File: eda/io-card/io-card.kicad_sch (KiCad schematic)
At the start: 22 parts, among them J3 PortA, J4 PortB, J5 ControlLines, J6 SPI, U1 W65C22SxP, U12 74HCT00, U2 W65C22SxP, U3 74HCT14, U4 74HCT14, U5 74HCT14, U8 74HCT138

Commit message: Add expansion backplane
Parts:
- removed H3, H4: MountingHole, MountingHole:MountingHole_2.5mm, symbol Mechanical:MountingHole
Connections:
- net at U2.7 (PA5): now also U8.3 (A2); no longer U8.1 (A0)
- net at U2.9 (PA7): now also U8.1 (A0); no longer U8.3 (A2)

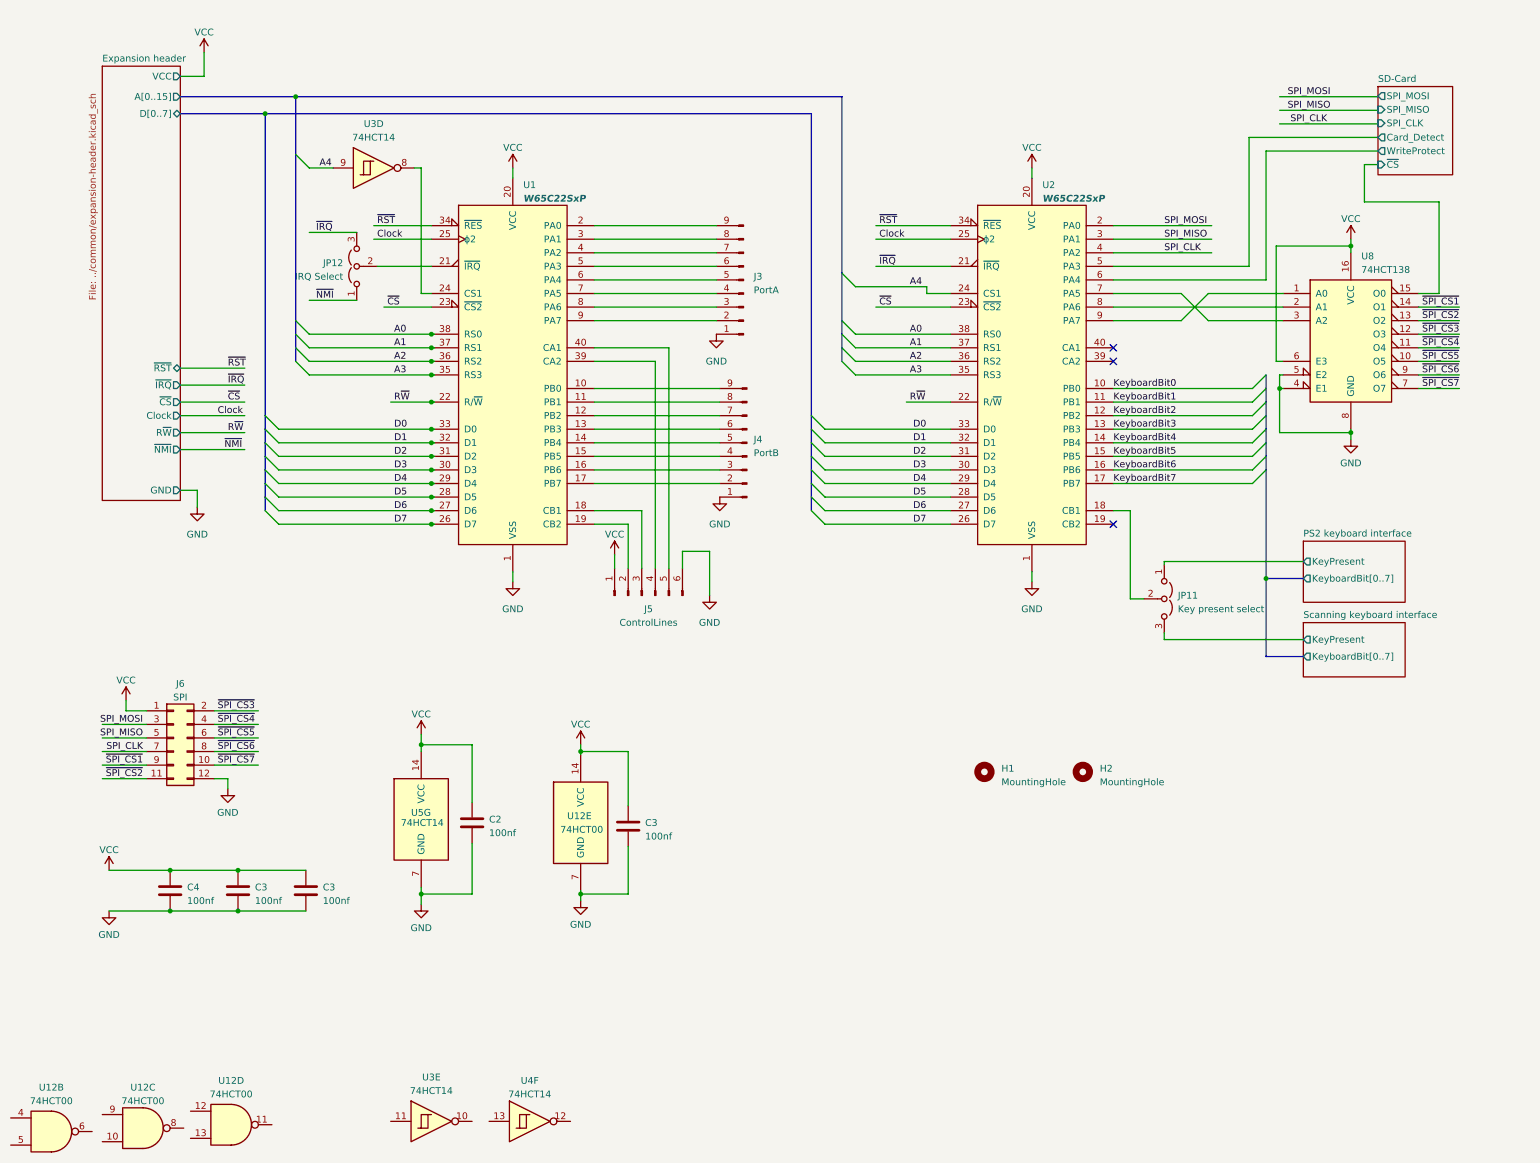
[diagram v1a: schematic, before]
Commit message: EDA work for new expansion header
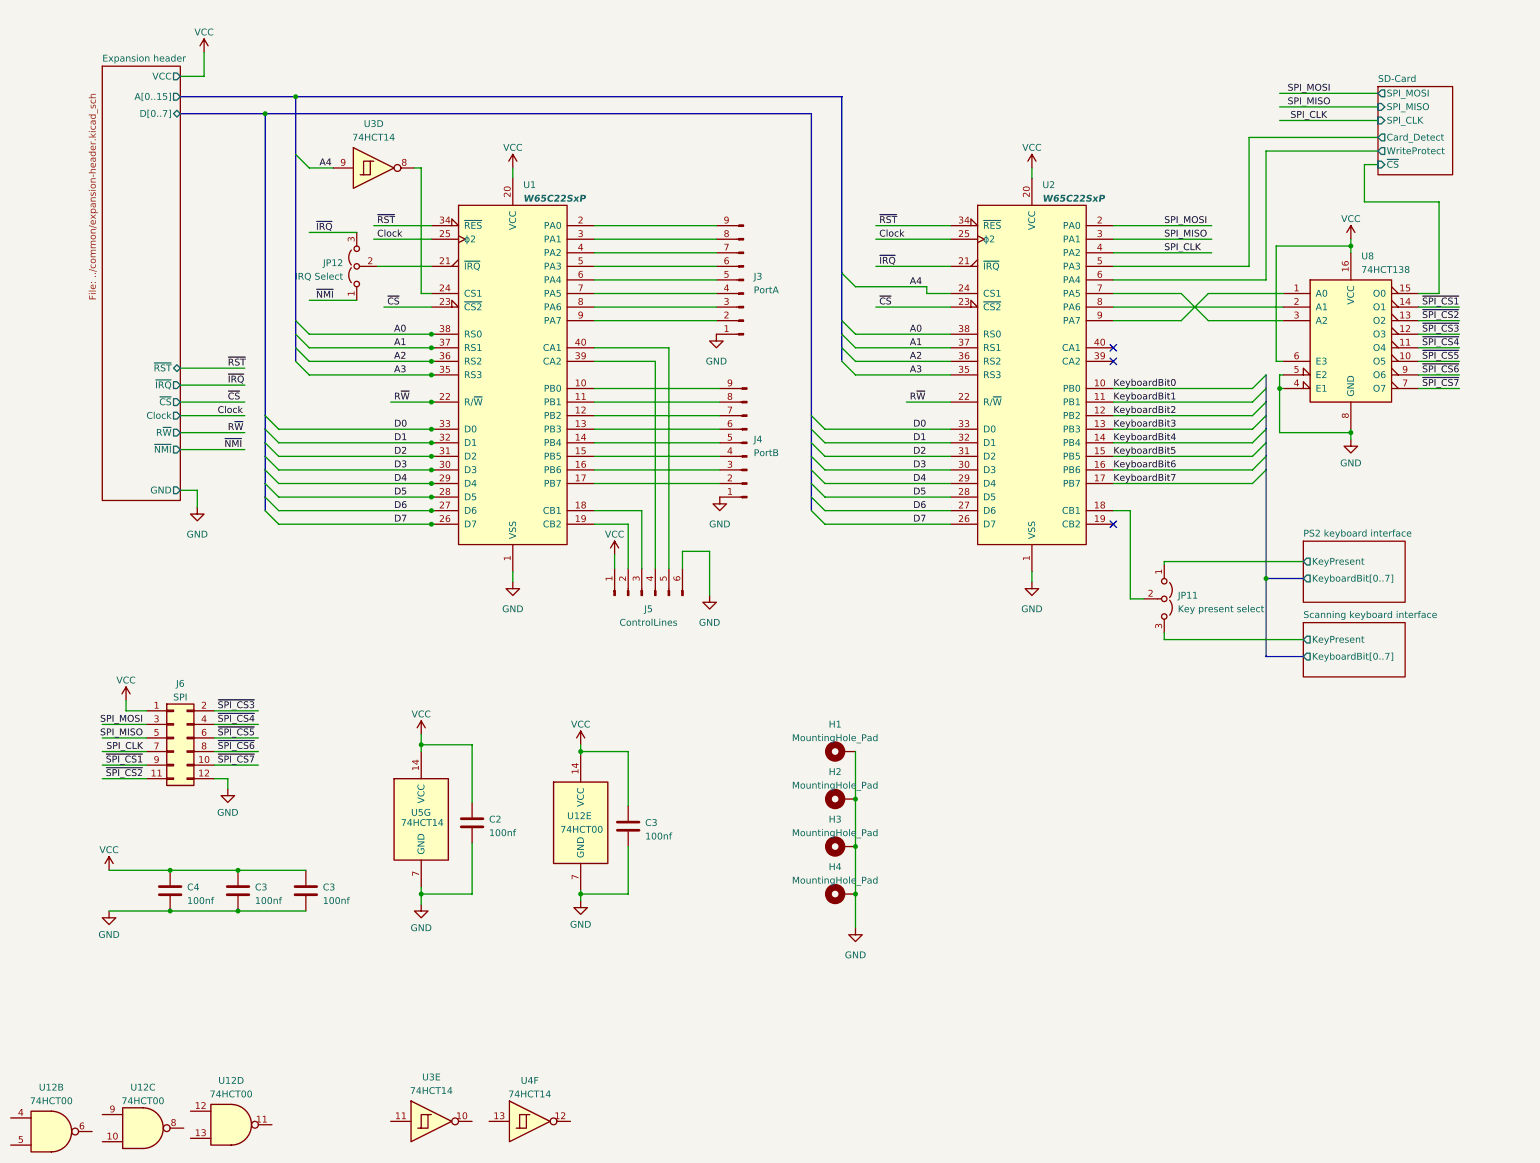
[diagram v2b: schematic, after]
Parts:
- removed H1, H2: MountingHole, MountingHole:MountingHole_2.5mm, symbol Mechanical:MountingHole
- added H1, H2, H3, H4: MountingHole_Pad, MountingHole:MountingHole_2.5mm_Pad, symbol Mechanical:MountingHole_Pad
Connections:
- net GND: now also H1.1, H2.1, H3.1, H4.1

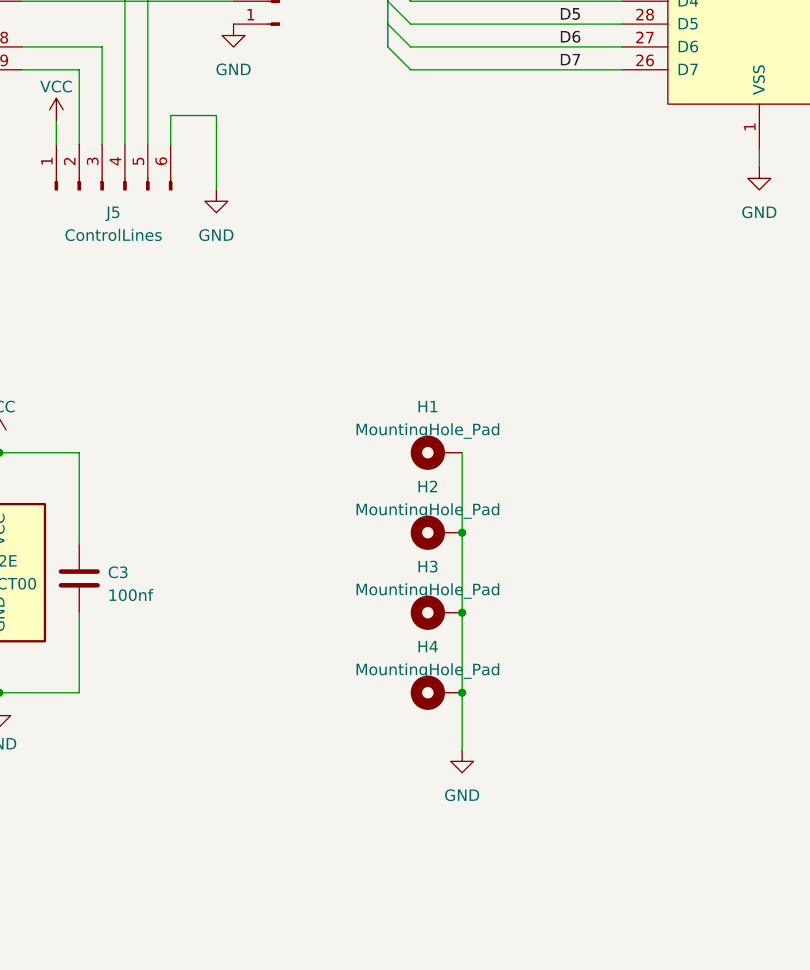
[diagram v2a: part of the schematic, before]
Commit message: Generate step files and start on gpu for new board layout
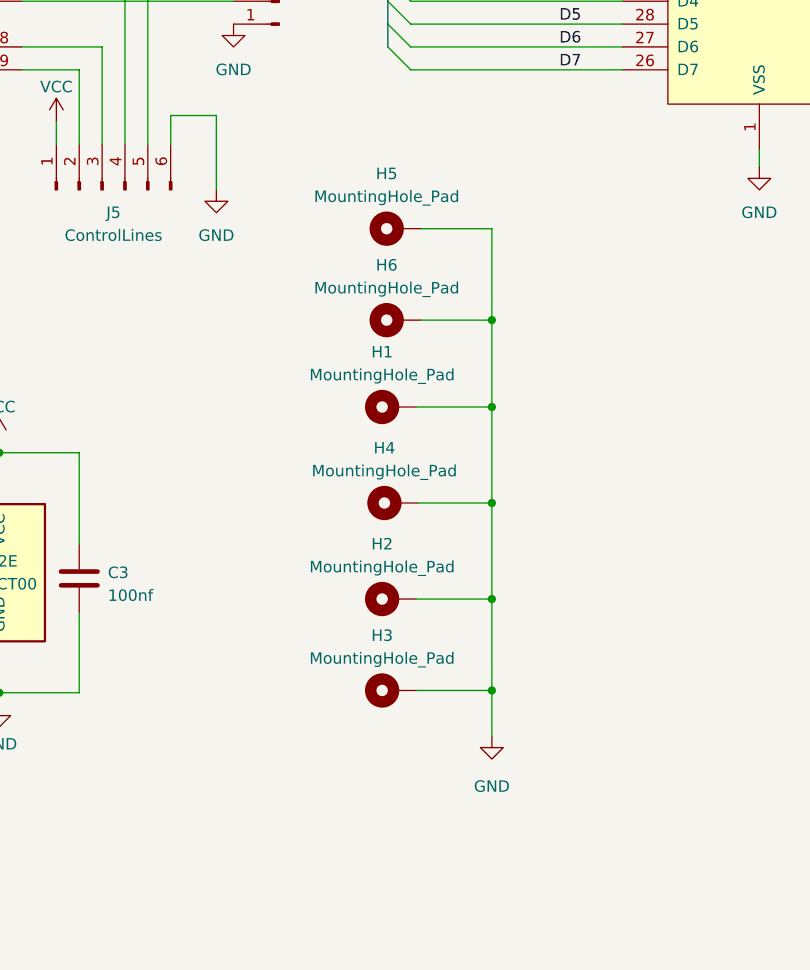
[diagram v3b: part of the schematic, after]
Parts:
- added H5, H6: MountingHole_Pad, MountingHole:MountingHole_2.5mm_Pad_Via, symbol Mechanical:MountingHole_Pad
- H1, H2, H3, H4: footprint MountingHole:MountingHole_2.5mm_Pad -> MountingHole:MountingHole_2.5mm_Pad_Via
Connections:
- net GND: now also H5.1, H6.1

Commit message: Normalize cap size
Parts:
- C2, C3, C4: footprint Capacitor_THT:C_Disc_D3.4mm_W2.1mm_P2.50mm -> Capacitor_THT:C_Disc_D3.8mm_W2.6mm_P2.50mm
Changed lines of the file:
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@@
       (effects (font (size 1.27 1.27)) (justify left))
     )
-    (property "Footprint" "Capacitor_THT:C_Disc_D3.4mm_W2.1mm_P2.50mm" (at 99.3902 173.355 0)
+    (property "Footprint" "Capacitor_THT:C_Disc_D3.8mm_W2.6mm_P2.50mm" (at 99.3902 173.355 0)
       (effects (font (size 1.27 1.27)) hide)
     )
@@
       (effects (font (size 1.27 1.27)) (justify left))
     )
-    (property "Footprint" "Capacitor_THT:C_Disc_D3.4mm_W2.1mm_P2.50mm" (at 55.5752 186.055 0)
+    (property "Footprint" "Capacitor_THT:C_Disc_D3.8mm_W2.6mm_P2.50mm" (at 55.5752 186.055 0)
       (effects (font (size 1.27 1.27)) hide)
     )
@@
       (effects (font (size 1.27 1.27)) (justify left))
     )
-    (property "Footprint" "Capacitor_THT:C_Disc_D3.4mm_W2.1mm_P2.50mm" (at 128.6002 173.99 0)
+    (property "Footprint" "Capacitor_THT:C_Disc_D3.8mm_W2.6mm_P2.50mm" (at 128.6002 173.99 0)
       (effects (font (size 1.27 1.27)) hide)
     )
@@
       (effects (font (size 1.27 1.27)) (justify left))
     )
-    (property "Footprint" "Capacitor_THT:C_Disc_D3.4mm_W2.1mm_P2.50mm" (at 42.8752 186.055 0)
+    (property "Footprint" "Capacitor_THT:C_Disc_D3.8mm_W2.6mm_P2.50mm" (at 42.8752 186.055 0)
       (effects (font (size 1.27 1.27)) hide)
     )
@@
       (effects (font (size 1.27 1.27)) (justify left))
     )
-    (property "Footprint" "Capacitor_THT:C_Disc_D3.4mm_W2.1mm_P2.50mm" (at 68.2752 186.055 0)
-      (effects (font (size 1.27 1.27)) hide)
-    )
+    (property "Footprint" "Capacitor_THT:C_Disc_D3.8mm_W2.6mm_P2.50mm" (at 68.2752 186.055 0)
+      (effects (font (size 1.27 1.27)) hide)
+    )

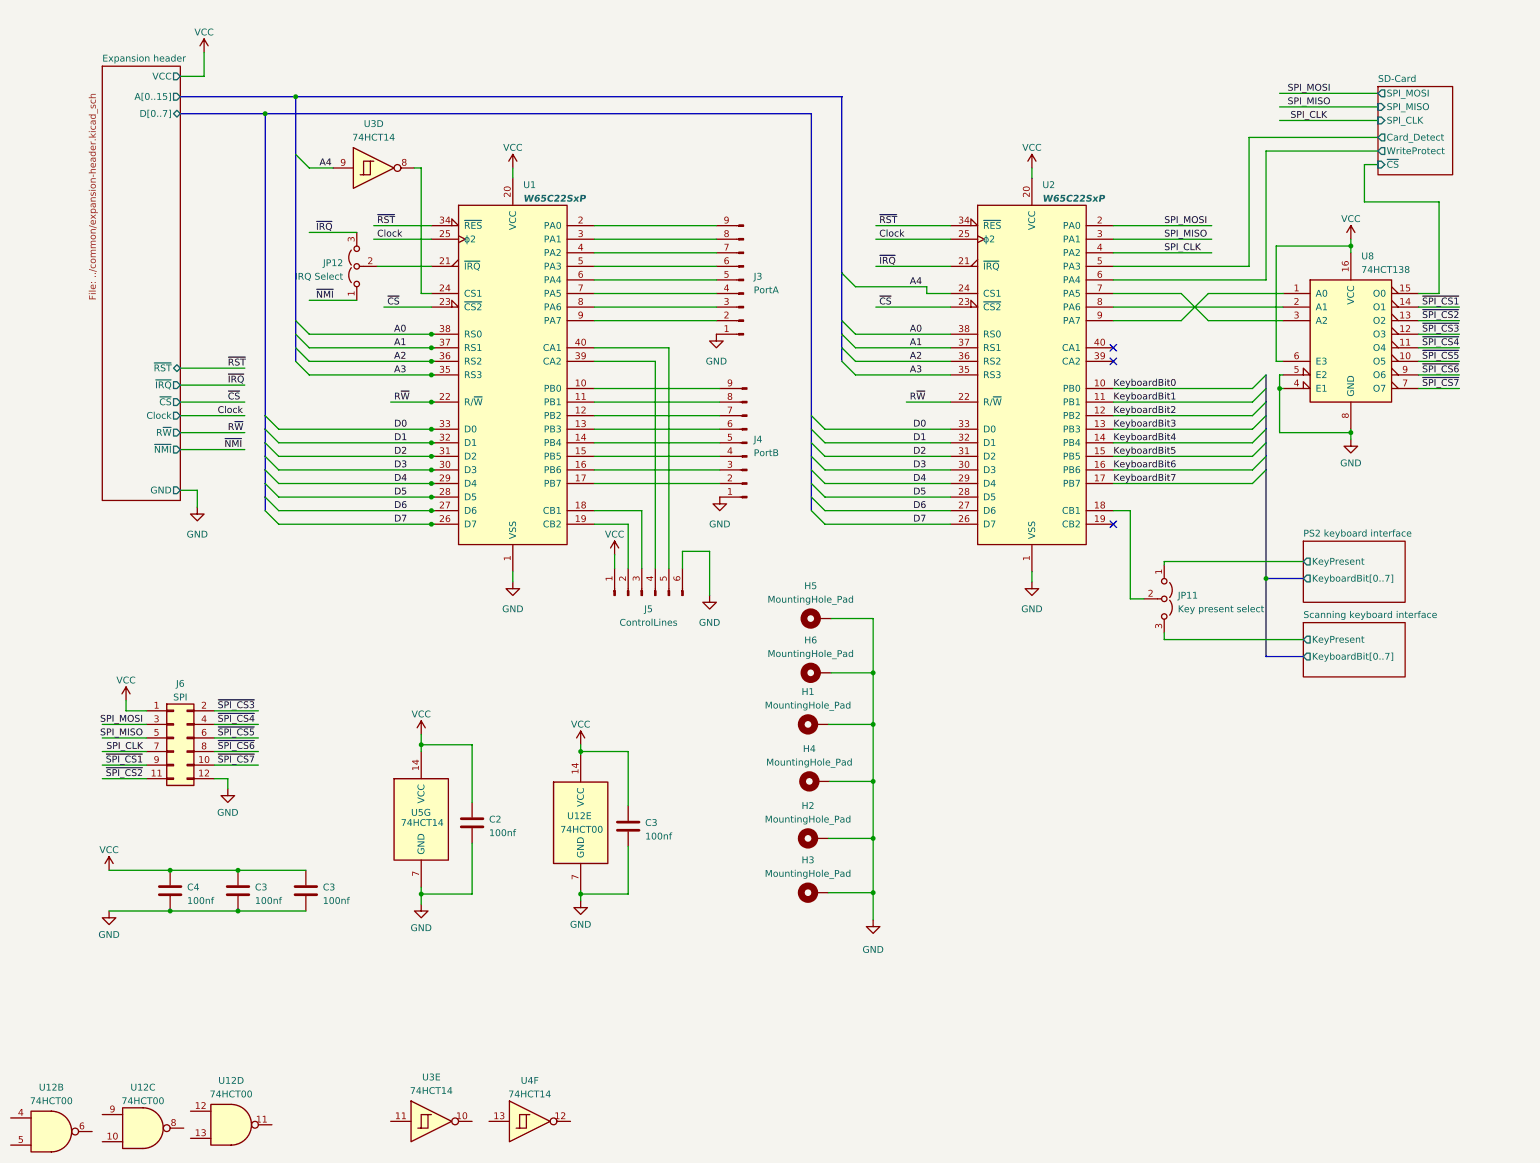
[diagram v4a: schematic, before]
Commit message: Rerouting IO card
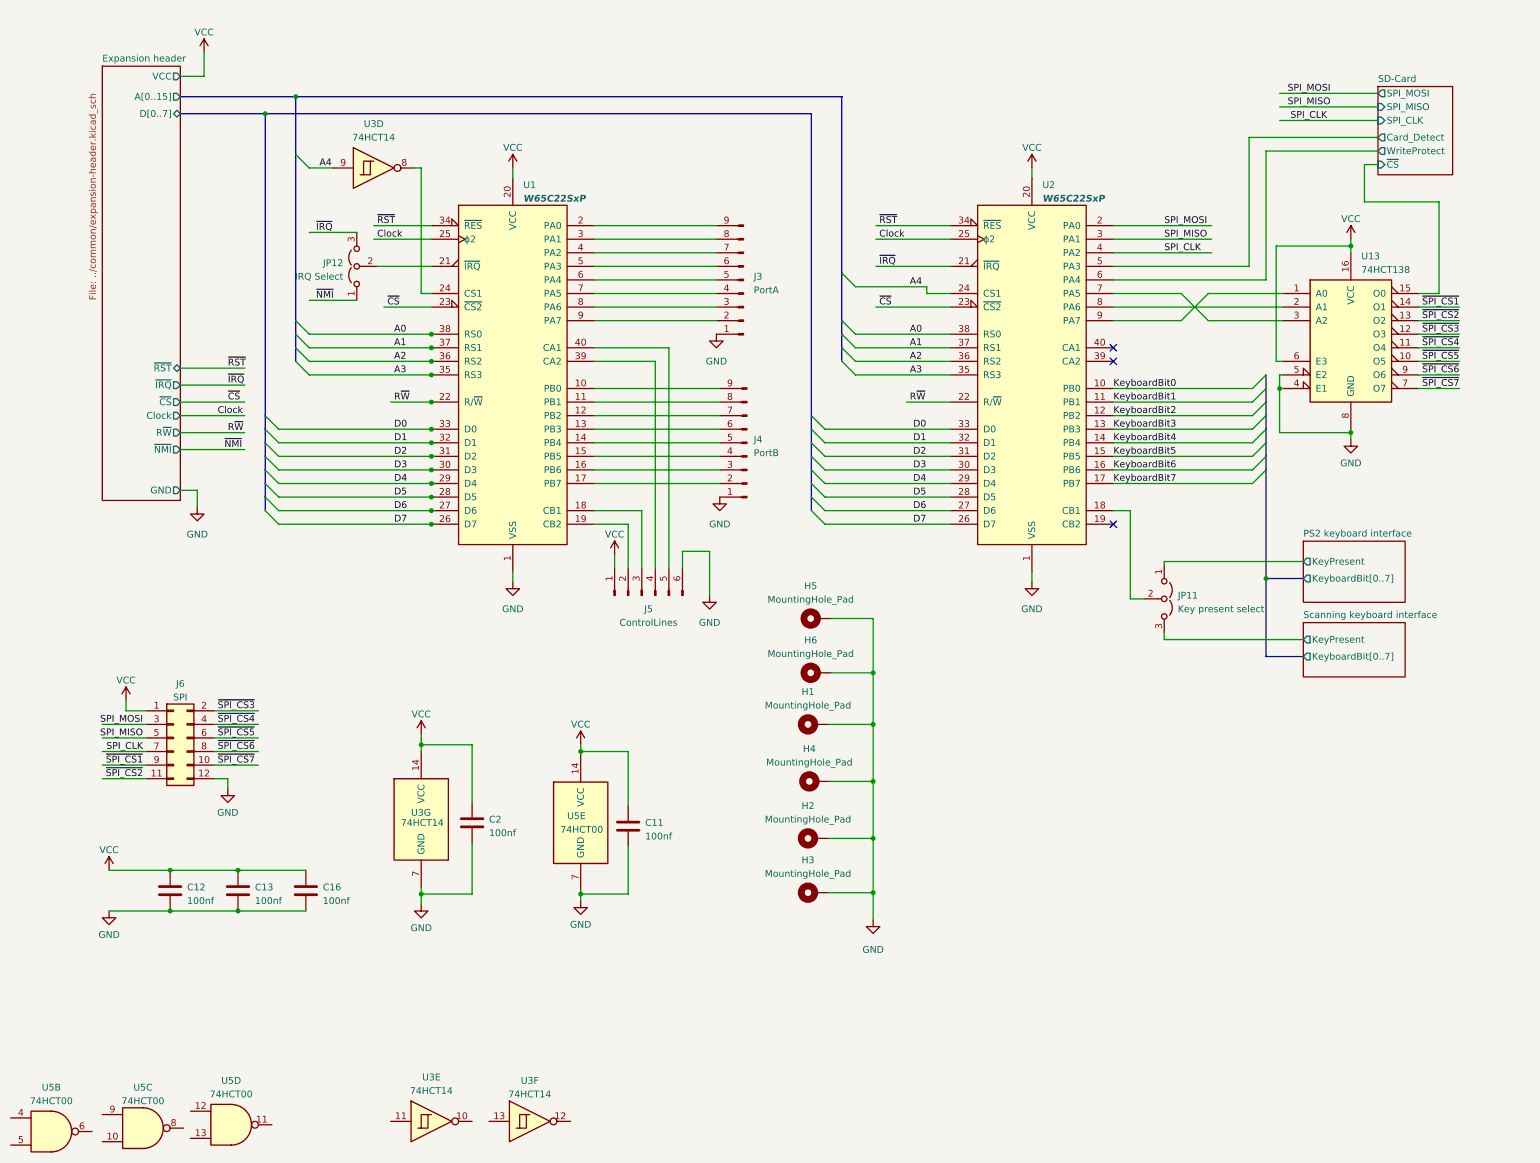
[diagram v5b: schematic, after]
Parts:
- J3, J4: footprint Connector_PinHeader_2.54mm:PinHeader_1x09_P2.54mm_Vertical -> Connector_PinHeader_2.54mm:PinHeader_1x09_P2.54mm_Horizontal
- J5: footprint Connector_PinHeader_2.54mm:PinHeader_1x06_P2.54mm_Vertical -> Connector_PinHeader_2.54mm:PinHeader_1x06_P2.54mm_Horizontal
- J6: footprint Connector_PinSocket_2.54mm:PinSocket_2x06_P2.54mm_Vertical -> Connector_PinHeader_2.54mm:PinHeader_2x06_P2.54mm_Horizontal
- renumbered C3 to C11, C4 to C12, C3 to C13, C3 to C16, U8 to U13, U5 to U3, U4 to U3, U12 to U5
